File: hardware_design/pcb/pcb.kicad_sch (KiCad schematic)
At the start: 15 parts, among them J1 Eurorack Power, Q1 DMG2305UX, U1 Pico, U2 PCM1808, U5 GY_PCM5102A, U6 APS6404L, U7 LM1117MP-5.0

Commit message: Rev 2 schematic & circuit board
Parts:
- removed C18, C19: 22u, Capacitor_SMD_AKL:CP_Elec_6.3x5.8, symbol Capacitor_AKL:CP_SMD_D6.3mm_H5.8mm
- removed C20: 100n, Capacitor_SMD_AKL:C_0603_1608Metric, symbol Capacitor_AKL:C_0603
- removed U7: LM1117MP-5.0, Package_TO_SOT_SMD:SOT-223-3_TabPin2, symbol Regulator_Linear:LM1117MP-5.0
- added U7: L7805, Package_TO_SOT_SMD:TO-252-2, symbol Regulator_Linear:L7805
- C1, C2: value CP_SMD_D6.3mm_H5.8mm -> 47u
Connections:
- net LED is gone; now on net I2S_DOUT: U1.10 (GPIO7)
- net +5V: now also U7.3 (OUT)
- net DIV_A: now also U1.5 (GPIO3); no longer U1.4 (GPIO2)
- net DIV_B: now also U1.6 (GPIO4); no longer U1.5 (GPIO3)
- net DIV_C: now also U1.7 (GPIO5); no longer U1.6 (GPIO4)
- net DIV_D: now also U1.9 (GPIO6); no longer U1.7 (GPIO5)
- net GND: now also U7.2 (GND)
- net I2S_BCK: now also U1.12 (GPIO9); no longer U1.11 (GPIO8)
- net I2S_DIN: now also U1.11 (GPIO8); no longer U1.15 (GPIO11)
- net I2S_DOUT: no longer U1.9 (GPIO6)
- net I2S_LRCK: now also U1.14 (GPIO10); no longer U1.12 (GPIO9)
- net I2S_SCK: now also U1.15 (GPIO11); no longer U1.14 (GPIO10)
- net VCC: now also U7.1 (IN)
- new net ALG_C: U1.4 (GPIO2)

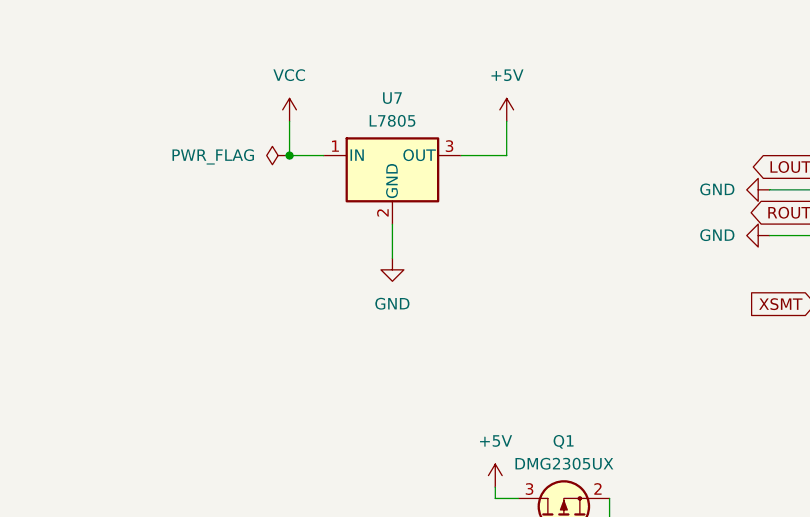
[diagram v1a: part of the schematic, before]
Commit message: Software switch de-bounce added as a result of Rev 2 testing.
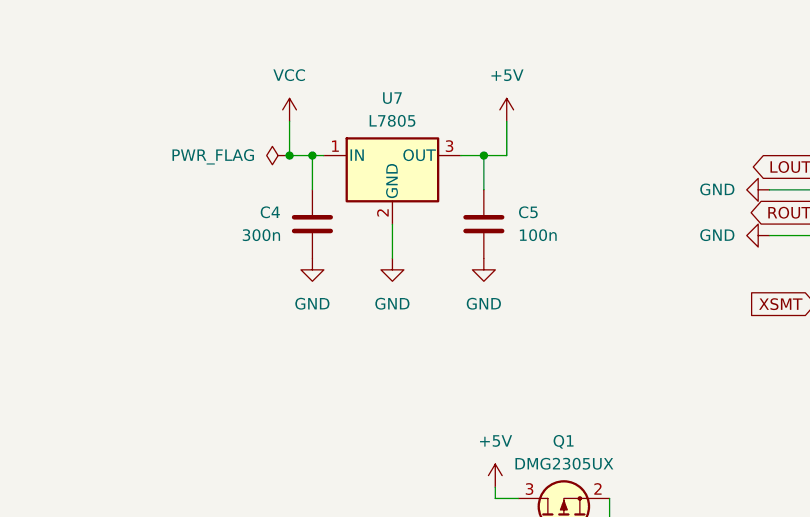
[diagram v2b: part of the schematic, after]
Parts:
- added C4: 300n, Capacitor_SMD_AKL:C_0603_1608Metric, symbol Capacitor_AKL:C_0603
- added C5: 100n, Capacitor_SMD_AKL:C_0603_1608Metric, symbol Capacitor_AKL:C_0603
- U7: footprint Package_TO_SOT_SMD:TO-252-2 -> DSP_CodecBoards:TO-252-2 with heatsink
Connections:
- net +5V: now also C5.1
- net GND: now also C4.2, C5.2
- net VCC: now also C4.1
